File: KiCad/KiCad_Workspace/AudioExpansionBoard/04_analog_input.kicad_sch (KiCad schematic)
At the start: 9 parts, among them U2 ADA4096-2ARMZ

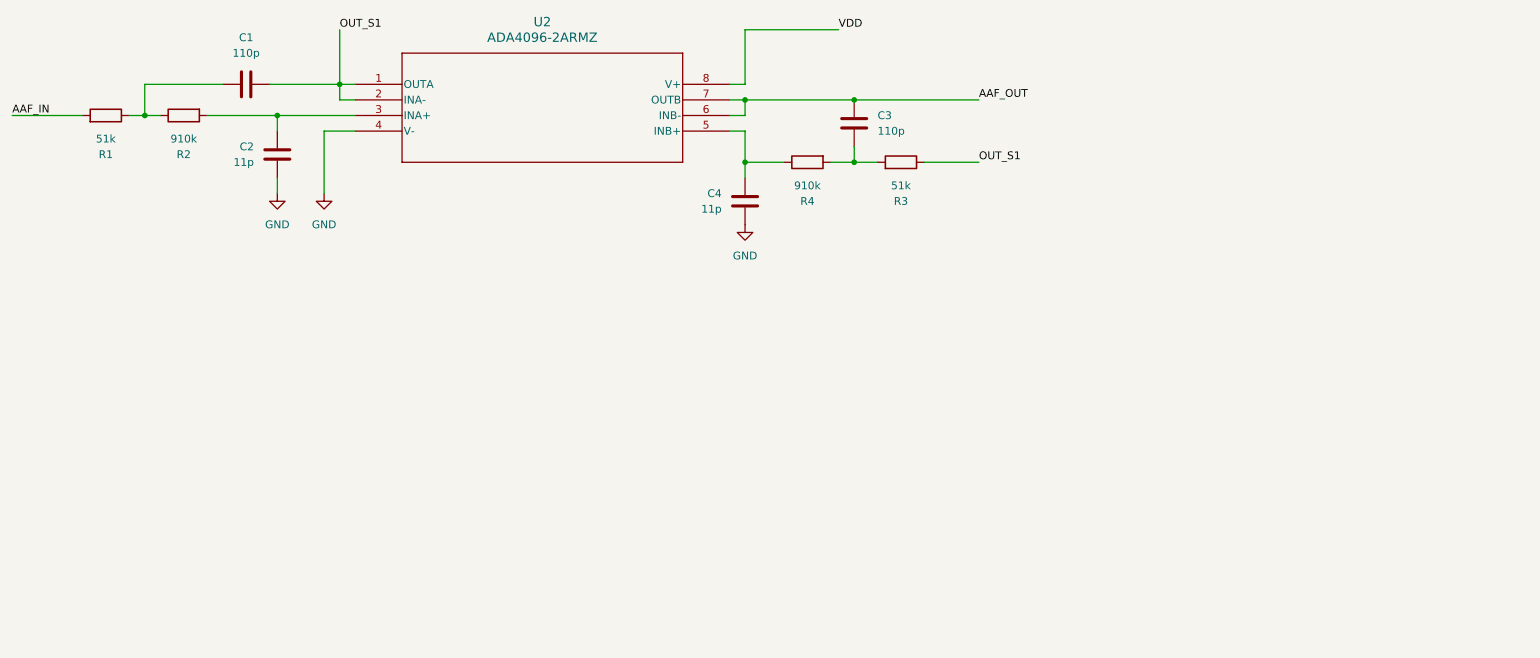
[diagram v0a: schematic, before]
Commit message: Added to analog line-in design schematic
Added schematic for more sections of analog line-in path (DC Blocker, Voltage Divider, ESD protection) with notes for each section and LTspice design schematics and simulation plots for each section of circuit added (although no simulation for combined sections yet)
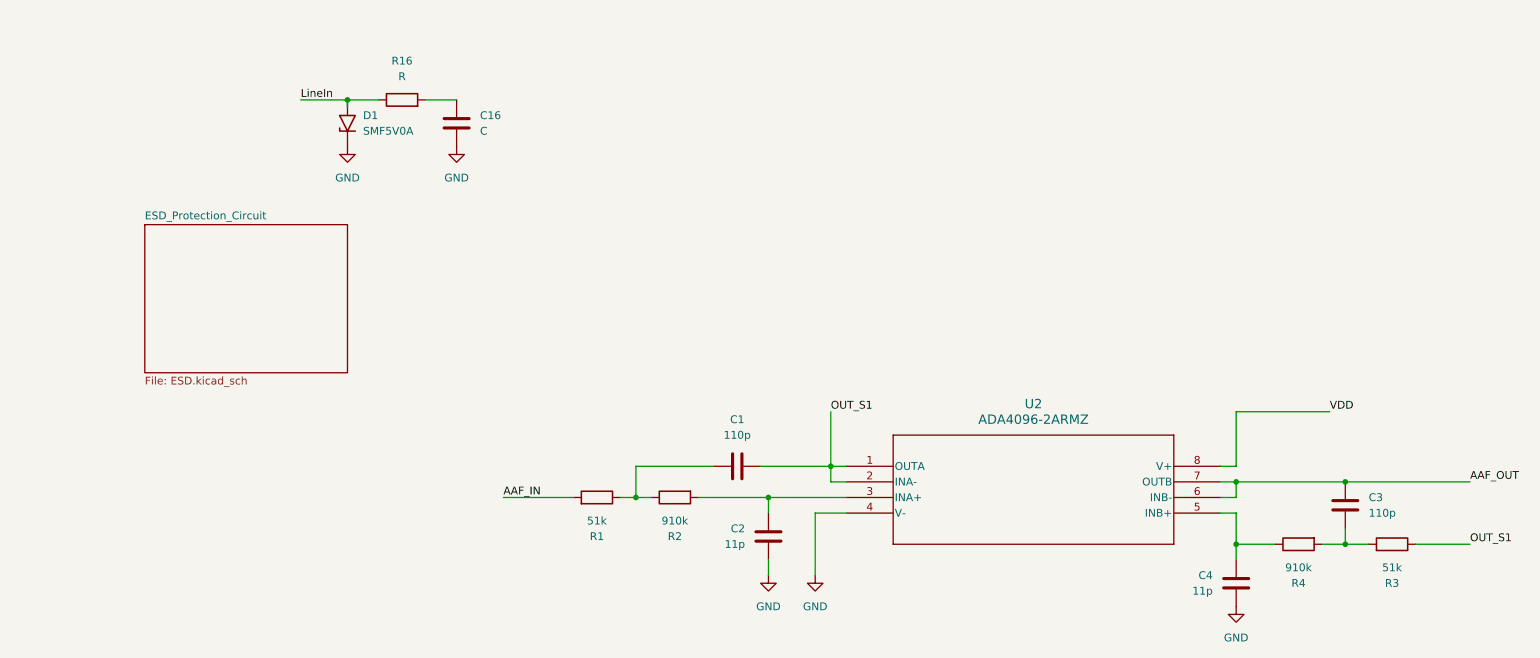
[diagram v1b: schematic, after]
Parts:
- added C16: C, symbol Device:C
- added D1: SMF5V0A, Diode_SMD:D_SMF, symbol Diode:SMF5V0A
- added R16: R, symbol Device:R
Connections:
- net GND: now also C16.2, D1.1 (A1)
- new net: C16.1, R16.2
- new net LineIn: D1.2 (A2), R16.1
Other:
- added sheet ESD_Protection_Circuit (ESD.kicad_sch)
- moved on the sheet: C1, C2, C3, C4, R1, R2, R3, R4, U2

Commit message: Added to designs to schematic and simulations
Added sections to analog line-in path (Offset and Voltage Divider). Moved the Sallen-Key Anti-Aliasing Filter to the line-in path schematic and added simulations (in LTspice) for each section of the analog line-in path.
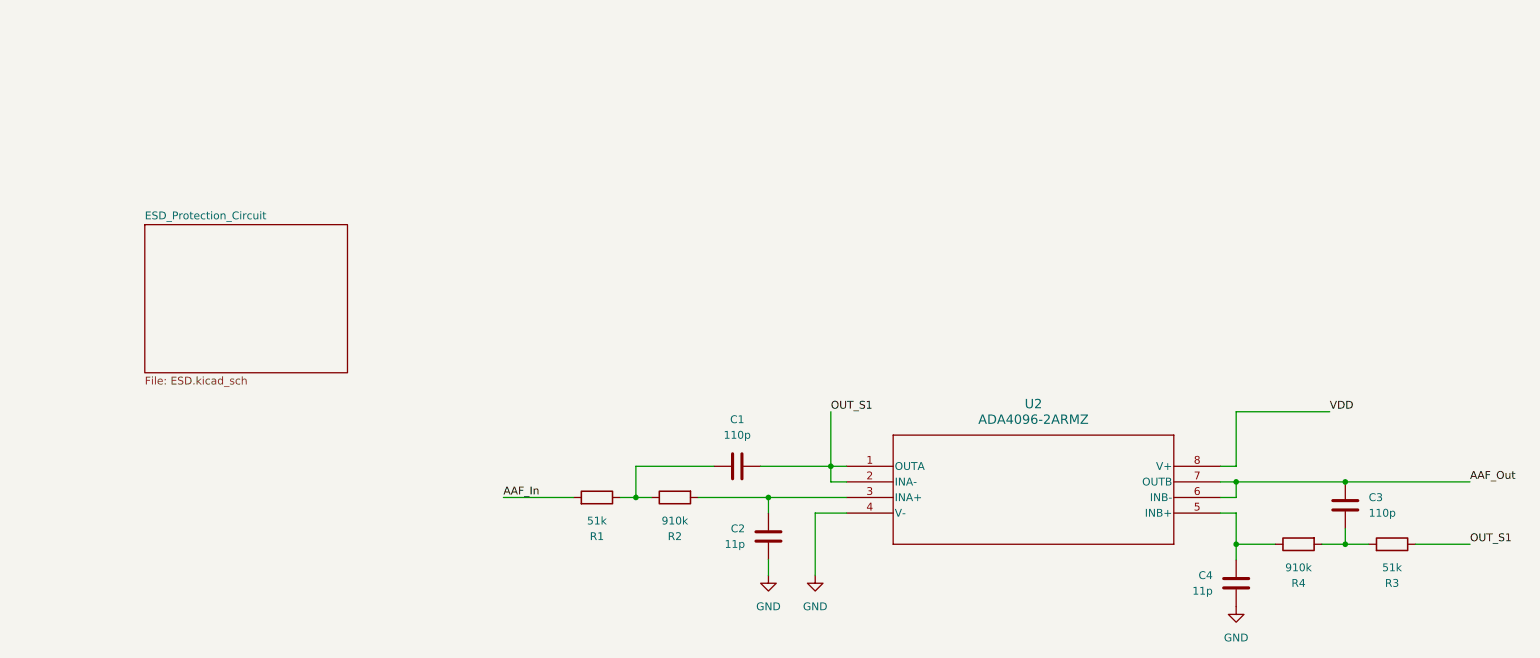
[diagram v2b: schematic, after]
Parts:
- removed C16: C, symbol Device:C
- removed D1: SMF5V0A, Diode_SMD:D_SMF, symbol Diode:SMF5V0A
- removed R16: R, symbol Device:R
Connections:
- net AAF_IN renamed AAF_In
- net AAF_OUT renamed AAF_Out
